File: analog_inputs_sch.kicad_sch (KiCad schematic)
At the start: 213 parts, among them J1 Conn_Coaxial, J2 Conn_Coaxial, J7 Conn_Coaxial, K3 TQ2-L2-5V, K4 TQ2-L2-5V, K6 TQ2-L2-5V, K7 TQ2-L2-5V, K8 TQ2-L2-5V, U1 OPA656U, U11 TL072, U13 TL072, U17 AD8611ARZ, U3 AD8337BCPZ-REEL-ND, U4 AD8138ARZ, U5 AD8337BCPZ-REEL-ND, U6 AD8138ARZ, U8 OPA656U

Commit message: Fix ERC
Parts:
- removed C103, C106: 100nF, Capacitor_SMD:C_0805_2012Metric, symbol Device:C
- removed C104, C107: 1uF, Capacitor_SMD:C_0805_2012Metric, symbol Device:C
- removed C105, C108: 10uF, Capacitor_SMD:C_0805_2012Metric, symbol Device:C
- removed L39, L41: LCBB-601, symbol Device:L
- removed L40, L42: 0.68uH, 0.8Ohm, symbol Device:L
- removed U13: TL072, symbol Amplifier_Operational:TL072

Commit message: Add all footprints
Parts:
- C11: renamed from C3; footprint Capacitor_SMD:C_0805_2012Metric -> Capacitor_SMD:C_Trimmer_Murata_TZB4-A
- C12: renamed from C59; footprint Capacitor_SMD:C_0805_2012Metric -> Capacitor_SMD:C_Trimmer_Murata_TZB4-A
- C3: renamed from C6; footprint Capacitor_SMD:C_0805_2012Metric -> Capacitor_SMD:C_Trimmer_Murata_TZB4-A
- C5: renamed from C7; footprint Capacitor_SMD:C_0805_2012Metric -> Capacitor_SMD:C_Trimmer_Murata_TZB4-A
- J1, J2: footprint AD813ARZ:R_8_ADI-L -> Connector_Coaxial:BNC_TEConnectivity_1478204_Vertical
- J3: renamed from J7; footprint (none) -> Connector_Coaxial:BNC_TEConnectivity_1478204_Vertical
- L1: renamed from L61; footprint (none) -> Inductor_SMD:L_0805_2012Metric
- L10: renamed from L47; footprint (none) -> Inductor_SMD:L_0805_2012Metric
- L11: renamed from L50; footprint (none) -> Inductor_SMD:L_0805_2012Metric
- L12: renamed from L48; footprint (none) -> Inductor_SMD:L_0805_2012Metric
- L13: renamed from L32; footprint (none) -> Inductor_SMD:L_0805_2012Metric
- L14: renamed from L28; footprint (none) -> Inductor_SMD:L_0805_2012Metric
- L15: renamed from L33; footprint (none) -> Inductor_SMD:L_0805_2012Metric
- L16: renamed from L29; footprint (none) -> Inductor_SMD:L_0805_2012Metric
- L17: renamed from L31; footprint (none) -> Inductor_SMD:L_0805_2012Metric
- L18: renamed from L27; footprint (none) -> Inductor_SMD:L_0805_2012Metric
- L19: renamed from L34; footprint (none) -> Inductor_SMD:L_0805_2012Metric
- L2: renamed from L59; footprint (none) -> Inductor_SMD:L_0805_2012Metric
- L20: renamed from L30; footprint (none) -> Inductor_SMD:L_0805_2012Metric
- L21: renamed from L57; footprint (none) -> Inductor_SMD:L_0805_2012Metric
- L22: renamed from L55; footprint (none) -> Inductor_SMD:L_0805_2012Metric
- L23: renamed from L58; footprint (none) -> Inductor_SMD:L_0805_2012Metric
- L24: renamed from L56; footprint (none) -> Inductor_SMD:L_0805_2012Metric
- L25: renamed from L19; footprint (none) -> Inductor_SMD:L_0805_2012Metric
- L26: renamed from L21; footprint (none) -> Inductor_SMD:L_0805_2012Metric
- L27: renamed from L23; footprint (none) -> Inductor_SMD:L_0805_2012Metric
- L28: renamed from L24; footprint (none) -> Inductor_SMD:L_0805_2012Metric
- L29: renamed from L20; footprint (none) -> Inductor_SMD:L_0805_2012Metric
- L3: renamed from L62; footprint (none) -> Inductor_SMD:L_0805_2012Metric
- L30: renamed from L22; footprint (none) -> Inductor_SMD:L_0805_2012Metric
- L31: renamed from L25; footprint (none) -> Inductor_SMD:L_0805_2012Metric
- L32: renamed from L26; footprint (none) -> Inductor_SMD:L_0805_2012Metric
- L4: renamed from L60; footprint (none) -> Inductor_SMD:L_0805_2012Metric
- L5: renamed from L53; footprint (none) -> Inductor_SMD:L_0805_2012Metric
- L6: renamed from L51; footprint (none) -> Inductor_SMD:L_0805_2012Metric
- L7: renamed from L54; footprint (none) -> Inductor_SMD:L_0805_2012Metric
- L8: renamed from L49; footprint (none) -> Inductor_SMD:L_0805_2012Metric
- L9: renamed from L52; footprint (none) -> Inductor_SMD:L_0805_2012Metric
- U1: renamed from U11; footprint (none) -> TL072:D8-L
- U4: renamed from U17; footprint (none) -> AD813ARZ:R_8_ADI-L
- U5: footprint footprints:CP_8_2_ADI -> AD8337BCPZ:CP_8_2_ADI-L
- U6: renamed from U3; footprint footprints:CP_8_2_ADI -> AD8337BCPZ:CP_8_2_ADI-L
- renumbered C56 to C1, C58 to C10, C1 to C13, C10 to C14, C143 to C15, C21 to C16, C144 to C17, C22 to C18, C145 to C19, C5 to C2, C142 to C20, C124 to C21, C121 to C22, C125 to C23, C122 to C24, C118 to C25, C115 to C26, C126 to C27, C123 to C28, C119 to C29, C116 to C30, C120 to C31, C117 to C32, C135 to C33, C131 to C34, C127 to C35, C132 to C36, C130 to C37, C93 to C38, C87 to C39, C2 to C4, C94 to C40, C133 to C41, C134 to C42, C92 to C43, C88 to C44, C86 to C45, C95 to C46, C89 to C47, C91 to C48, C85 to C49, C96 to C50, C90 to C51, C13 to C52, C12 to C53, C72 to C54, C75 to C55, C137 to C56, C136 to C57, C14 to C58, C79 to C59, C8 to C6, C139 to C60, C138 to C61, C73 to C62, C76 to C63, C80 to C64, C81 to C65, C74 to C66, C77 to C67, C82 to C68, C83 to C69, C4 to C7, C11 to C70, C84 to C71, C26 to C72, C23 to C73, C28 to C74, C29 to C75, C57 to C8, D2 to D1, D1 to D2, K6 to K1, K3 to K2, K7 to K3, K8 to K5, R8 to R1, R15 to R10, R2 to R11, R16 to R12, R94 to R13, R110 to R14, R53 to R15, R112 to R16, R39 to R17, R109 to R18, R111 to R19, R3 to R2, R38 to R20, R45 to R21, R41 to R22, R37 to R23, R23 to R24, R33 to R25, R200 to R26, R44 to R27, R29 to R28, R31 to R29, R1 to R3, R28 to R30, R34 to R31, R20 to R32, R30 to R33, R43 to R34, R199 to R35, R17 to R36, R7 to R37, R198 to R38, R35 to R39, R12 to R4, R18 to R40, R19 to R41, R6 to R42, R69 to R43, R21 to R44, R22 to R45, R24 to R46, R25 to R47, R26 to R48, R27 to R49, R9 to R5, R5 to R50, R4 to R51, R32 to R52, R36 to R53, R71 to R54, R70 to R55, R13 to R6, R10 to R7, R11 to R8, R14 to R9, TP4 to TP10, TP15 to TP11, TP16 to TP12, TP17 to TP13, TP18 to TP14, TP19 to TP15, TP20 to TP16, TP22 to TP17, TP21 to TP18, TP25 to TP19, TP7 to TP2, TP26 to TP20, TP23 to TP21, TP24 to TP22, TP2 to TP3, TP8 to TP4, TP9 to TP5, TP3 to TP6, TP5 to TP7, TP11 to TP8, TP13 to TP9, U8 to U2, U1 to U3, U6 to U7, U4 to U8
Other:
- note added: "TODO: choose C trimmer"

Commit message: Apply changes after review, left to fix: comparator histeresis, PSU missing lines?
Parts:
- removed K1, K2, K3, K4, K5: TQ2-L2-5V, TQ2:RELAY_TQ2_2C_PAN, symbol 2025-10-25_18-45-48:TQ2-L2-5V
- removed R14, R16, R18, R19: 10k, Resistor_SMD:R_0805_2012Metric, symbol Device:R
- added C140, C141: 100pF, Capacitor_SMD:C_0805_2012Metric, symbol Device:C
- added K1, K2, K3, K4, K5, K6, K7, K8: TQ2-5V, TQ2-5V:TQ2, symbol TQ2-5V:TQ2-5V
- added R57, R66: 10R, Resistor_SMD:R_0805_2012Metric, symbol Device:R
- C11, C12: value C 2.0 - 6.0 pF -> 2.0-6.0pF
- C3, C5: value C 2.0 - 10.0 pF -> 2.0-10.0pF
- C4, C6: value C 360 pF -> 360pF
- C7, C9: value C 390 pF -> 390pF
- R1, R2: value R 953k -> 990k
- R10, R8: value R 953k -> 953k
- R31, R32: value 10k -> 2M
- R5, R6: value R 9.53 kΩ -> 10k
- R7, R9: value R 49.9k -> 49.9k
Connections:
- net +5V_EXT: now also K1.1, K2.1, K3.1, K4.1, K6.1, K7.1, K8.1
- net AC_DC_CH1: now also K2.10
- net AC_DC_CH2: now also K7.10
- net AN_TRIGGER_CH1: now also K3.2
- net AN_TRIGGER_CH2: now also K3.4
- net EXT_TRIGGER_LEVEL: now also K4.4
- net GND: now also U5.2 (VCOM), U6.2 (VCOM), C140.1, C141.1
- net TRIGGER_AC_DC: now also K4.10
- net TRIGG_1: now also K3.10
- net TRIGG_2: now also K8.10
- net at R28.1, R30.1, U5.4 (INPN): no longer U5.2 (VCOM)
- net at C13.1, R11.2, TP3.1: now also K2.3
- net at C10.1, C12.1, C9.2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: now also K2.7
- net at C2.1, C5.1, R2.1: now also K1.2
- net at R4.2, TP2.1: now also K1.3
- net at C9.1, R9.1: now also K1.4
- net at R12.1: now also K2.8
- net at C2.2, C5.2, C6.1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: now also K2.9
- net at C13.2, D2.6 (K3A4), TP6.1: now also U3.3 (POS), K2.2
- net at U1.6 (-), U1.7: now also R66.2; no longer R15.2, TP8.1
- net at C14.1, R12.2, TP4.1: now also K7.3
- net at C7.1, R7.1: now also K6.4
- net at C11.1, C7.2, C8.1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: now also K1.7
- net at C33.2, R25.2, TP11.1: now also K5.4
- net at R17.2, TP7.1: now also C140.2, R57.1; no longer U1.1, U1.2 (-)
- net at U2.3 (POS): now also C14.2, D1.6 (K3A4), TP5.1, K7.2
- net at C1.2, C3.2, C4.1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: now also K1.9
- net at C33.1: now also K4.3, K5.3
- net at C1.1, C3.1, R1.1: now also K6.2
- net at R3.2, TP1.1: now also K6.3
- net at R11.1: now also K1.8
- net at R29.1, R33.1, U6.4 (INPN): no longer U6.2 (VCOM)
- net +1V5 renamed +1V5_VOCM_CH1
- net +1V5_VOCM_CH1: no longer C53.1, U8.2 (VOCM)
- new net: C141.2, R15.2, R66.1, TP8.1
- new net: K3.3, K4.2
- new net: R57.2, U1.1, U1.2 (-)
- new net +1V5_VOCM_CH2: C53.1, U8.2 (VOCM)
- new net CH1_ATTEN: K6.10
- new net CH2_ATTEN: K1.10
- no-connect marks 10 -> 20
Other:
- note added: "1 : 100"
- note added: "RELAY COILS"
- note added: "TODO: What R20 for histeresis?"
- note removed: "~ 1 : 100"
- moved on the sheet: C1, C15, C16, C17, C18, C19, C20, C8, J3, L1, L2, L3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

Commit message: Fix footprints and allign components placements
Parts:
- removed K8: TQ2-5V, TQ2-5V:TQ2, symbol TQ2-5V:TQ2-5V
- added unit 3 of K5
- added unit 1 of K5
- U2, U3: footprint OPA656U:SOIC127P599X175-8N -> OPA656:SOIC127P599X175-8N
- U4: footprint AD813ARZ:R_8_ADI-L -> AD8611ARZ:R_8_ADI-L
- U7, U8: footprint AD813ARZ:R_8_ADI-L -> AD8138ARZ:R_8_ADI-L
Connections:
- net +5V_EXT: now also K5.1
- net AC_DC_CH1: now also K3.10; no longer K2.10
- net AC_DC_CH2: now also K4.10; no longer K7.10
- net AN_TRIGGER_CH1: now also K5.2; no longer K3.2
- net AN_TRIGGER_CH2: now also K5.4; no longer K3.4
- net CH1_ATTEN: now also K1.10; no longer K6.10
- net CH2_ATTEN: now also K2.10; no longer K1.10
- net EXT_TRIGGER_LEVEL: now also K6.4; no longer K4.4
- net TRIGGER_AC_DC: now also K7.10; no longer K4.10
- net TRIGG_1: now also K5.10; no longer K3.10
- net TRIGG_2: now also K6.10
- net at C13.1, R11.2, TP3.1: now also K3.3; no longer K2.3
- net at C13.2, D2.6 (K3A4), TP6.1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: now also K3.2; no longer K2.2
- net at R4.2, TP2.1: now also K2.3; no longer K1.3
- net at C14.1, R12.2, TP4.1: now also K4.3; no longer K7.3
- net at C2.1, C5.1, R2.1: now also K2.2; no longer K1.2
- net at C33.2, R25.2, TP11.1: now also K7.2; no longer K5.4
- net at K4.2: now also C14.2, D1.6 (K3A4), TP5.1, U2.3 (POS); no longer K3.3
- net at C1.1, C3.1, R1.1: now also K1.2; no longer K6.2
- net at C9.1, R9.1: now also K2.4; no longer K1.4
- net at C7.1, R7.1: now also K1.4; no longer K6.4
- net at R3.2, TP1.1: now also K1.3; no longer K6.3
- new net: K5.3, K6.2
- new net: C33.1, K6.3, K7.3

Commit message: Save work before adding symetrical op amp
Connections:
- net CH1_CH+ renamed CH1_CH_P
- net CH1_CH- renamed CH1_CH_N
- net CH2_CH+ renamed CH2_CH_P
- net CH2_CH- renamed CH2_CH_N
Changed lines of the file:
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@@
 		)
 	)
-	(global_label "CH2_CH-"
+	(global_label "CH2_CH_N"
 		(shape output)
 		(at 779.78 351.79 0)
@@
 		)
 		(property "Intersheetrefs" "${INTERSHEET_REFS}"
-			(at 791.7157 351.79 0)
+			(at 792.4414 351.79 0)
 			(effects
 				(font
@@
 		)
 	)
-	(global_label "CH1_CH+"
+	(global_label "CH1_CH_P"
 		(shape output)
 		(at 777.24 203.2 0)
@@
 		)
 		(property "Intersheetrefs" "${INTERSHEET_REFS}"
-			(at 789.1757 203.2 0)
+			(at 789.8409 203.2 0)
 			(effects
 				(font
@@
 		)
 	)
-	(global_label "CH1_CH-"
+	(global_label "CH1_CH_N"
 		(shape output)
 		(at 777.24 213.36 0)
@@
 		)
 		(property "Intersheetrefs" "${INTERSHEET_REFS}"
-			(at 789.1757 213.36 0)
+			(at 789.9014 213.36 0)
 			(effects
 				(font
@@
 		)
 	)
-	(global_label "CH2_CH+"
+	(global_label "CH2_CH_P"
 		(shape output)
 		(at 779.78 341.63 0)
@@
 		)
 		(property "Intersheetrefs" "${INTERSHEET_REFS}"
-			(at 791.7157 341.63 0)
+			(at 792.3809 341.63 0)
 			(effects
 				(font
@@
 		)
 		(property "Value" "20k"
-			(at 385.572 352.806 90)
+			(at 386.842 352.806 90)
 			(effects
 				(font

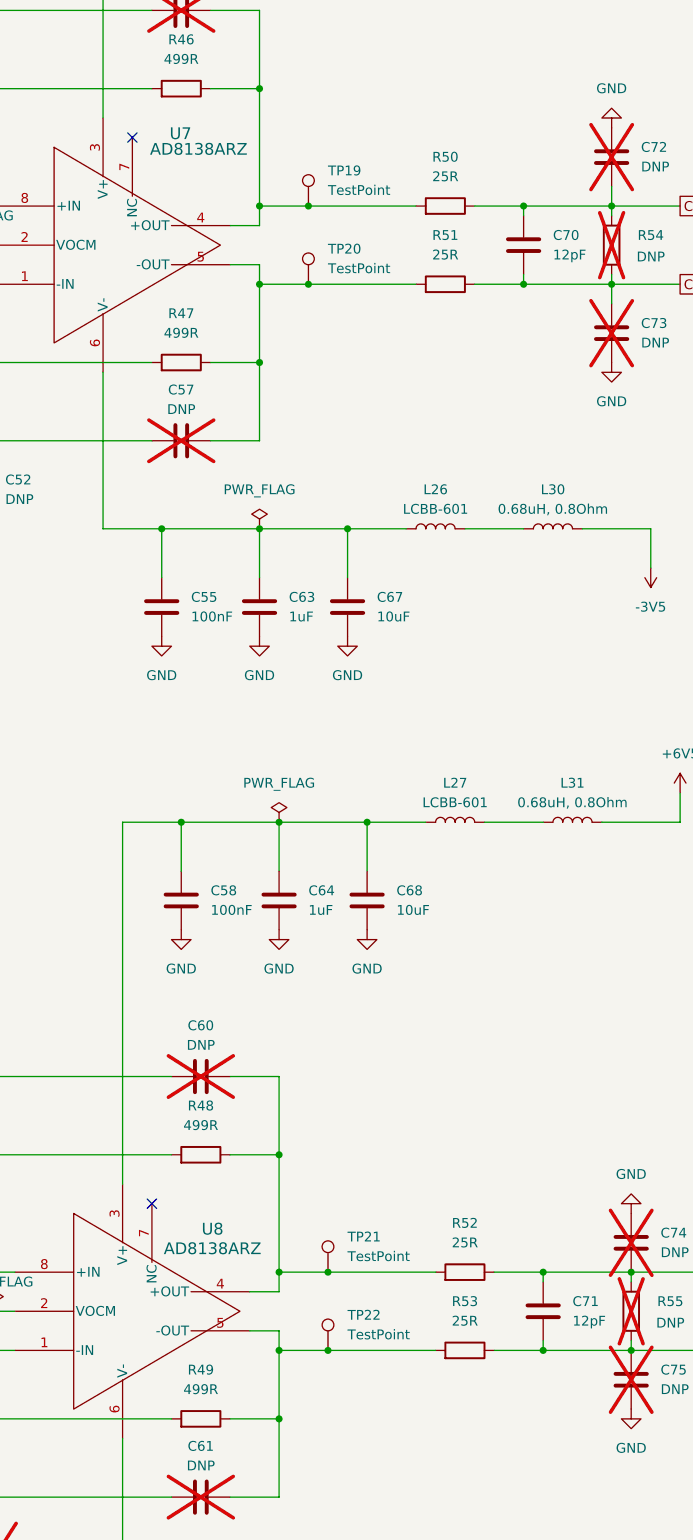
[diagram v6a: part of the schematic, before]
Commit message: Add LDO's
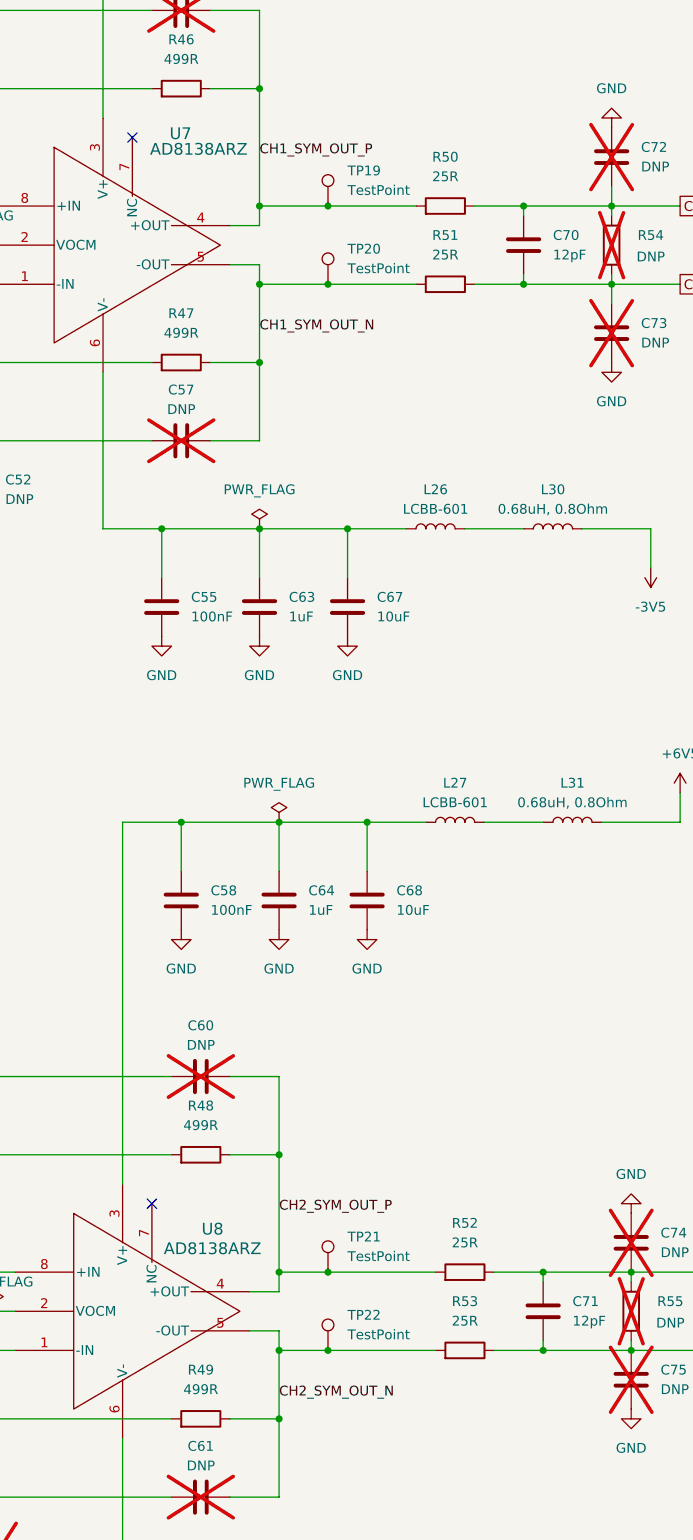
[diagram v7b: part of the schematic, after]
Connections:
- net CH1_SYM_OUT_P: now reaches C56.2, R46.1, R50.2, TP19.1, U7.4 (+OUT)
- net CH2_SYM_OUT_P: now reaches C60.2, R48.1, R52.2, TP21.1, U8.4 (+OUT)
- net CH2_SYM_OUT_N: now reaches C61.2, R49.1, R53.2, TP22.1, U8.5 (-OUT)
- net CH1_SYM_OUT_N: now reaches C57.2, R47.1, R51.2, TP20.1, U7.5 (-OUT)
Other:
- moved on the sheet: TP19, TP20
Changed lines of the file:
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@@
 	)
 	(junction
+		(at 731.52 213.36)
+		(diameter 0)
+		(color 0 0 0 0)
+	)
+	(junction
 		(at 154.94 127)
 		(diameter 0)
@@
 	)
 	(junction
-		(at 728.98 203.2)
-		(diameter 0)
-		(color 0 0 0 0)
-	)
-	(junction
 		(at 497.84 506.73)
 		(diameter 0)
@@
 	)
 	(junction
+		(at 731.52 203.2)
+		(diameter 0)
+		(color 0 0 0 0)
+	)
+	(junction
 		(at 73.66 360.68)
 		(diameter 0)
@@
 	)
 	(junction
-		(at 728.98 213.36)
-		(diameter 0)
-		(color 0 0 0 0)
-	)
-	(junction
 		(at 421.64 193.04)
 		(diameter 0)
@@
 	(wire
 		(pts
-			(xy 392.43 300.99) (xy 381 300.99)
+			(xy 731.52 203.2) (xy 742.95 203.2)
 		)
 		(stroke
@@
 	(wire
 		(pts
-			(xy 756.92 213.36) (xy 756.92 212.09)
+			(xy 392.43 300.99) (xy 381 300.99)
 		)
 		(stroke
@@
 	(wire
 		(pts
-			(xy 728.98 213.36) (xy 742.95 213.36)
+			(xy 756.92 213.36) (xy 756.92 212.09)
 		)
 		(stroke
@@
 	(wire
 		(pts
-			(xy 722.63 213.36) (xy 728.98 213.36)
+			(xy 722.63 213.36) (xy 731.52 213.36)
 		)
 		(stroke
@@
 	(wire
 		(pts
+			(xy 731.52 213.36) (xy 742.95 213.36)
+		)
+		(stroke
+			(width 0)
+			(type default)
+		)
+	)
+	(wire
+		(pts
 			(xy 759.46 351.79) (xy 759.46 350.52)
 		)
@@
 	(wire
 		(pts
-			(xy 722.63 203.2) (xy 728.98 203.2)
+			(xy 722.63 203.2) (xy 731.52 203.2)
 		)
 		(stroke
@@
 	(wire
 		(pts
-			(xy 728.98 203.2) (xy 742.95 203.2)
-		)
-		(stroke
-			(width 0)
-			(type default)
-		)
-	)
-	(wire
-		(pts
 			(xy 180.34 68.58) (xy 180.34 67.31)
 		)
@@
 		)
 	)
+	(label "CH1_SYM_OUT_N"
+		(at 722.63 219.71 0)
+		(effects
+			(font
+				(size 1.27 1.27)
+			)
+			(justify left bottom)
+		)
+	)
+	(label "CH2_SYM_OUT_N"
+		(at 725.17 358.14 0)
+		(effects
+			(font
+				(size 1.27 1.27)
+			)
+			(justify left bottom)
+		)
+	)
+	(label "CH2_SYM_OUT_P"
+		(at 725.17 334.01 0)
+		(effects
+			(font
+				(size 1.27 1.27)
+			)
+			(justify left bottom)
+		)
+	)
+	(label "CH1_SYM_OUT_P"
+		(at 722.63 196.85 0)
+		(effects
+			(font
+				(size 1.27 1.27)
+			)
+			(justify left bottom)
+		)
+	)
 	(global_label "AN_TRIGGER_N"
 		(shape output)
@@
 	(symbol
 		(lib_id "Connector:TestPoint")
-		(at 728.98 213.36 0)
+		(at 731.52 213.36 0)
 		(unit 1)
 		(exclude_from_sim no)
@@
 		(fields_autoplaced yes)
 		(property "Reference" "TP20"
-			(at 731.52 208.7879 0)
+			(at 734.06 208.7879 0)
 			(effects
 				(font
@@
 		)
 		(property "Value" "TestPoint"
-			(at 731.52 211.3279 0)
+			(at 734.06 211.3279 0)
 			(effects
 				(font
@@
 		)
 		(property "Footprint" "Connector_PinHeader_2.54mm:PinHeader_1x01_P2.54mm_Vertical"
-			(at 734.06 213.36 0)
+			(at 736.6 213.36 0)
 			(effects
 				(font
@@
 		)
 		(property "Datasheet" "~"
-			(at 734.06 213.36 0)
+			(at 736.6 213.36 0)
 			(effects
 				(font
@@
 		)
 		(property "Description" "test point"
-			(at 728.98 213.36 0)
+			(at 731.52 213.36 0)
 			(effects
 				(font
@@
 	(symbol
 		(lib_id "Connector:TestPoint")
-		(at 728.98 203.2 0)
+		(at 731.52 203.2 0)
 		(unit 1)
 		(exclude_from_sim no)
@@
 		(fields_autoplaced yes)
 		(property "Reference" "TP19"
-			(at 731.52 198.6279 0)
+			(at 734.06 198.6279 0)
 			(effects
 				(font
@@
 		)
 		(property "Value" "TestPoint"
-			(at 731.52 201.1679 0)
+			(at 734.06 201.1679 0)
 			(effects
 				(font
@@
 		)
 		(property "Footprint" "Connector_PinHeader_2.54mm:PinHeader_1x01_P2.54mm_Vertical"
-			(at 734.06 203.2 0)
+			(at 736.6 203.2 0)
 			(effects
 				(font
@@
 		)
 		(property "Datasheet" "~"
-			(at 734.06 203.2 0)
+			(at 736.6 203.2 0)
 			(effects
 				(font
@@
 		)
 		(property "Description" "test point"
-			(at 728.98 203.2 0)
+			(at 731.52 203.2 0)
 			(effects
 				(font

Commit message: Place all componenets
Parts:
- renumbered C2 to C1, C8 to C10, C12 to C11, C11 to C12, C140 to C15, C141 to C16, C15 to C17, C16 to C18, C21 to C19, C1 to C2, C22 to C20, C17 to C21, C18 to C22, C19 to C26, C26 to C27, C20 to C28, C27 to C29, C5 to C3, C28 to C30, C29 to C31, C30 to C32, C31 to C33, C32 to C34, C33 to C35, C34 to C36, C35 to C37, C36 to C38, C37 to C39, C6 to C4, C38 to C40, C39 to C41, C40 to C42, C41 to C43, C42 to C44, C43 to C45, C44 to C46, C45 to C47, C46 to C48, C47 to C49, C3 to C5, C48 to C50, C49 to C51, C50 to C52, C51 to C53, C52 to C54, C53 to C55, C54 to C56, C55 to C57, C56 to C58, C57 to C59, C4 to C6, C58 to C60, C59 to C61, C60 to C62, C61 to C63, C62 to C64, C63 to C65, C64 to C66, C65 to C67, C66 to C68, C67 to C69, C9 to C7, C68 to C70, C69 to C71, C70 to C72, C71 to C73, C72 to C74, C73 to C75, C74 to C76, C75 to C77, C10 to C8, C7 to C9, K2 to K1, K1 to K2, K4 to K3, K3 to K4, L5 to L3, L6 to L4, L3 to L5, L4 to L6, R2 to R1, R7 to R10, R8 to R11, R11 to R13, R57 to R14, R66 to R15, R15 to R16, R20 to R18, R21 to R19, R1 to R2, R22 to R20, R23 to R21, R24 to R22, R25 to R23, R26 to R24, R27 to R25, R28 to R26, R29 to R27, R30 to R28, R31 to R29, R6 to R3, R32 to R30, R33 to R31, R34 to R32, R35 to R33, R36 to R34, R37 to R35, R38 to R36, R39 to R37, R40 to R38, R41 to R39, R5 to R4, R42 to R40, R43 to R41, R44 to R42, R45 to R43, R46 to R44, R47 to R45, R48 to R46, R49 to R47, R50 to R48, R51 to R49, R3 to R5, R52 to R50, R53 to R51, R54 to R52, R55 to R53, R4 to R6, R13 to R7, R9 to R8, R10 to R9
